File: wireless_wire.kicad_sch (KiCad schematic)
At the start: 21 parts, among them SW1 SW_Push, SW2 SW_Push, U2 TLV75533PDBV, U3 ESP32-S3-WROOM-1, X1 USB4085-GF-A

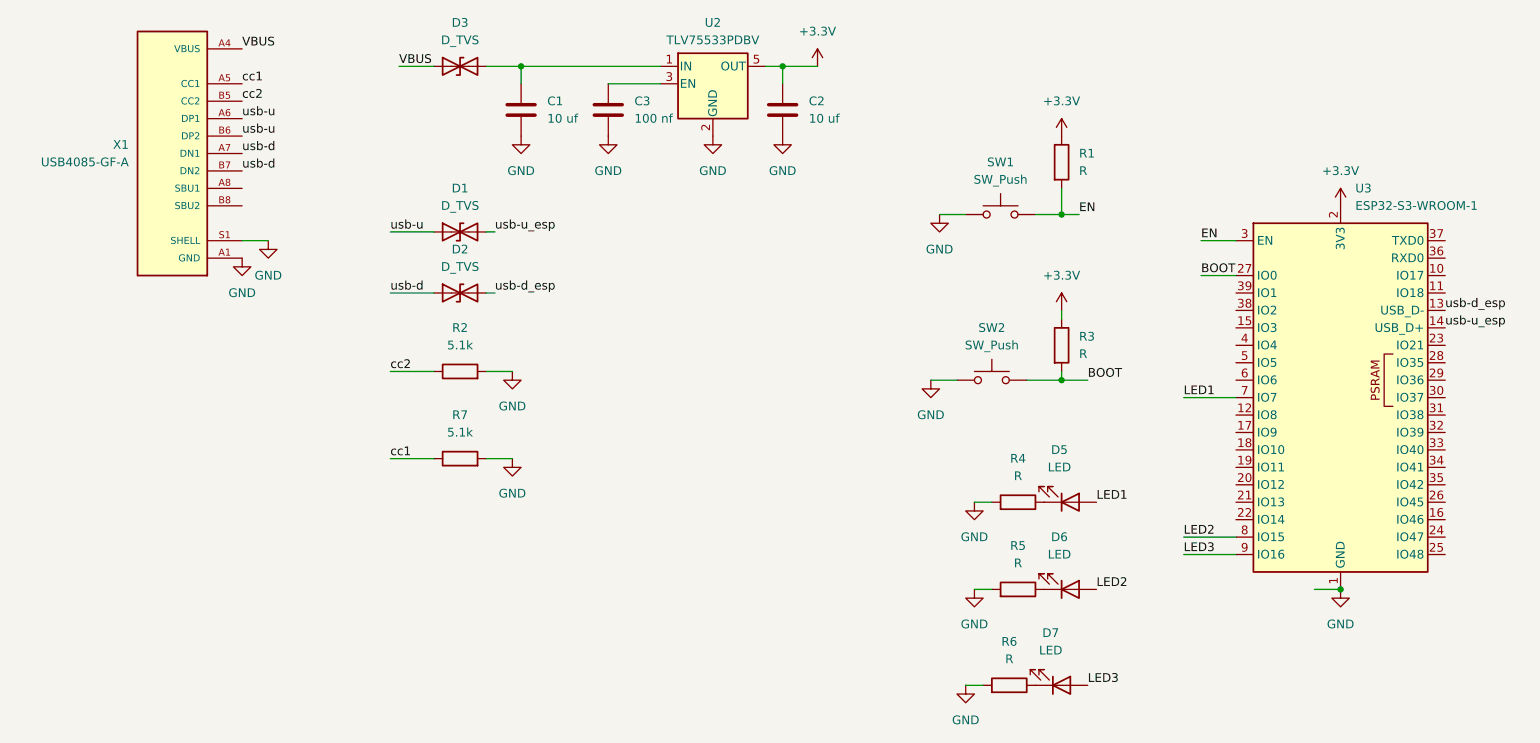
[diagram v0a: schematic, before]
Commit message: fixed silkscreen and BOM finished
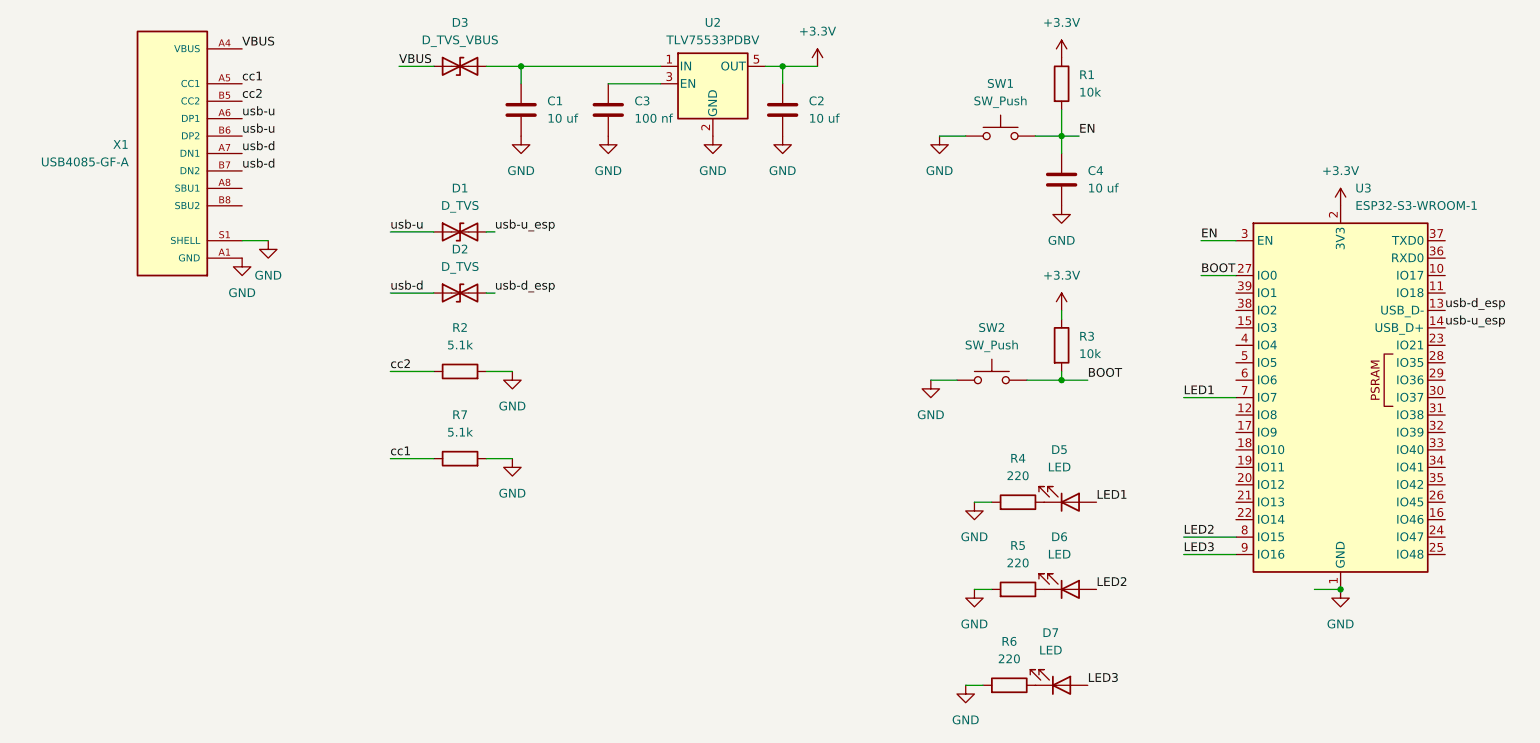
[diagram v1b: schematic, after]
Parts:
- added C4: 10 uf, Capacitor_SMD:C_0805_2012Metric, symbol Device:C
- D3: value D_TVS -> D_TVS_VBUS
- R1, R3: value R -> 10k
- R4, R5, R6: value R -> 220
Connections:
- net EN: now also C4.1
- net GND: now also C4.2
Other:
- moved on the sheet: R1, SW1
